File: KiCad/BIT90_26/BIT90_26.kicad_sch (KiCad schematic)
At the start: 0 parts

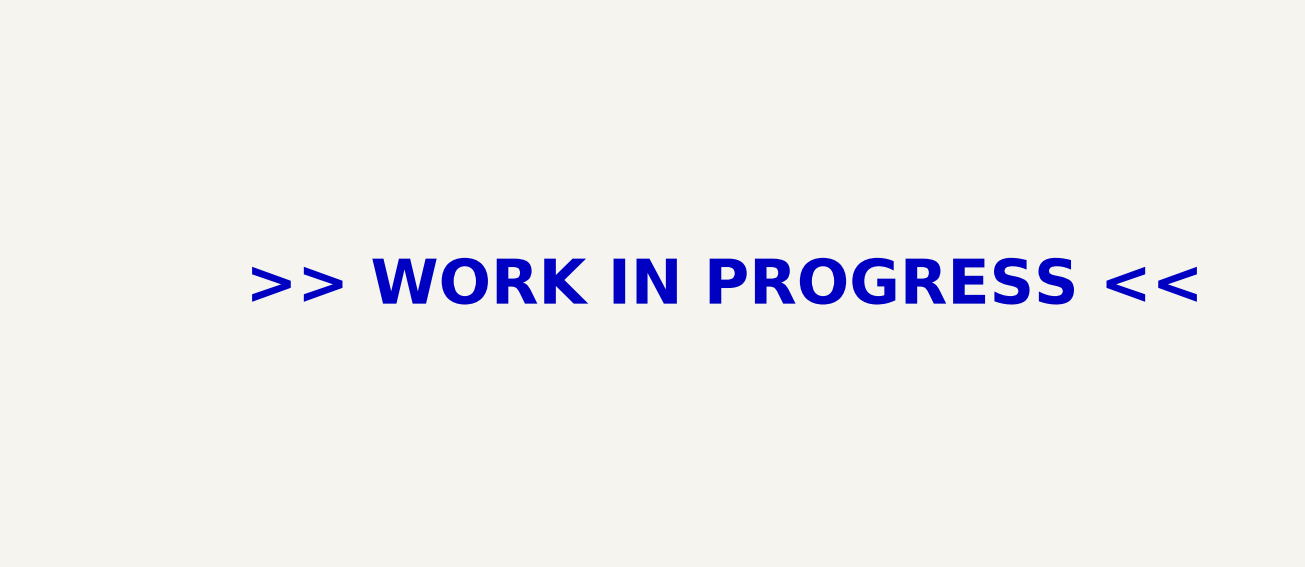
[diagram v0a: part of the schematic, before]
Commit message: Minor corrections & footprints assigned
PCB layout started
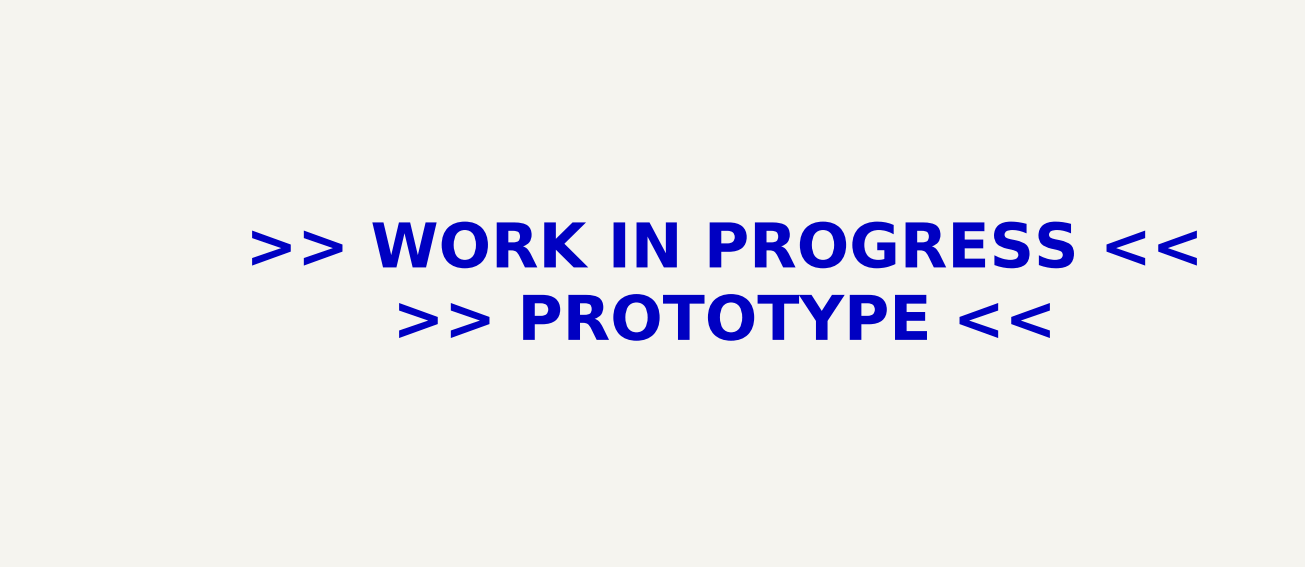
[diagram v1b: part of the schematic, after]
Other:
- note added: ">> WORK IN PROGRESS << >> PROTOTYPE <<"
- note removed: ">> WORK IN PROGRESS <<"
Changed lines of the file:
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@@
 	(title_block
 		(title "BIT90/26 Computer")
-		(date "5/JUN/2026")
+		(date "6/JUN/2026")
 		(rev "WIP")
 		(company "Brett Hallen")
@@
 		(comment 4 "Based on original schematics from BIT Corporation (普澤有限公司)")
 	)
-	(text ">> WORK IN PROGRESS <<"
+	(text ">> WORK IN PROGRESS <<\n>> PROTOTYPE <<"
 		(exclude_from_sim no)
 		(at 282.956 186.944 0)
